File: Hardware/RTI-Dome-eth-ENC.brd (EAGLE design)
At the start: 119.4 x 71.1 mm, 87 parts, among them IC1 24AA128ST, IC3 FT232RL, IC4 REG1117, IC5 74LVC245, IC6 74ABT245, J1 POWERPOLE_POWER45A, U1 W5500, X13 PN61729-S, X9 J1011F21PNL

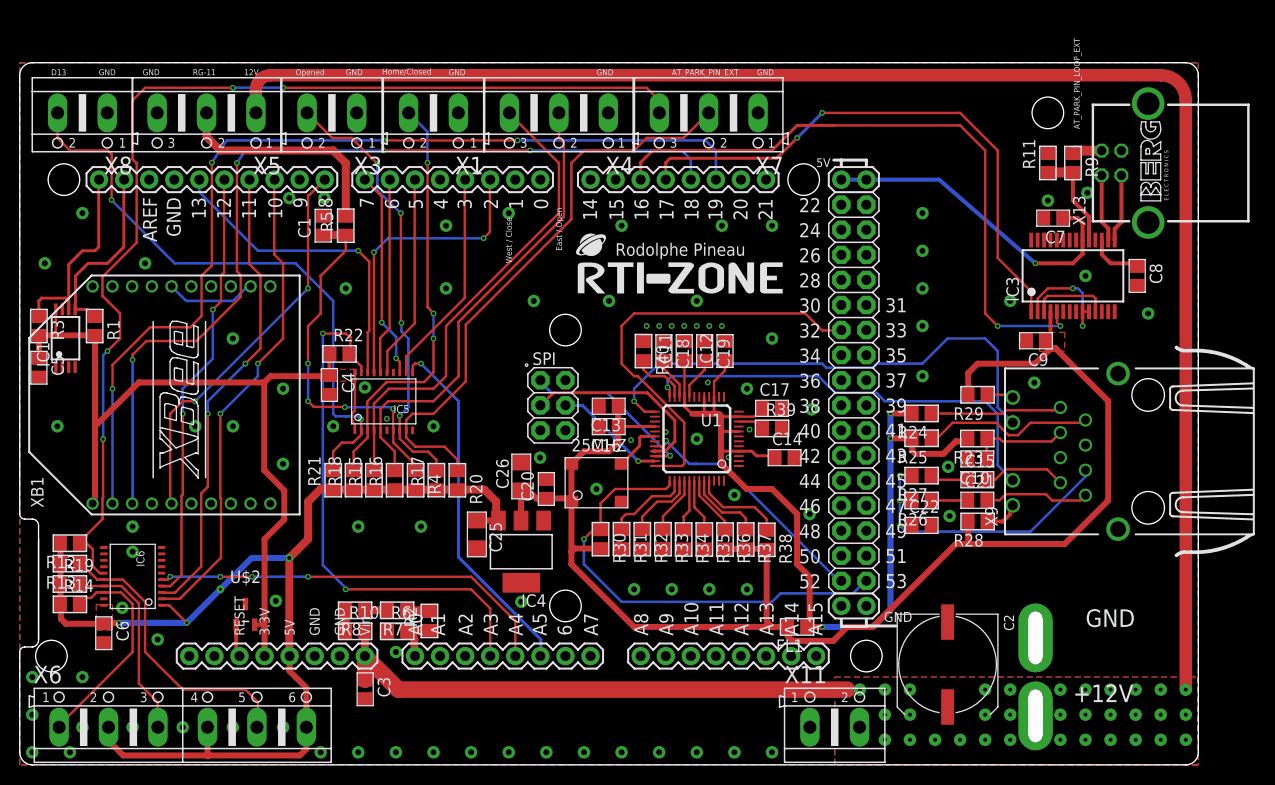
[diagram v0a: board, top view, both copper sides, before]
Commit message: Better homing code. Does necessarily stop at home bug sinf home via an interrupt. I'll add more got to go back home after passing it. It does however return the proper position after homing. Added more board for ENC424J600 ethernet chip. Fix position of the headers.
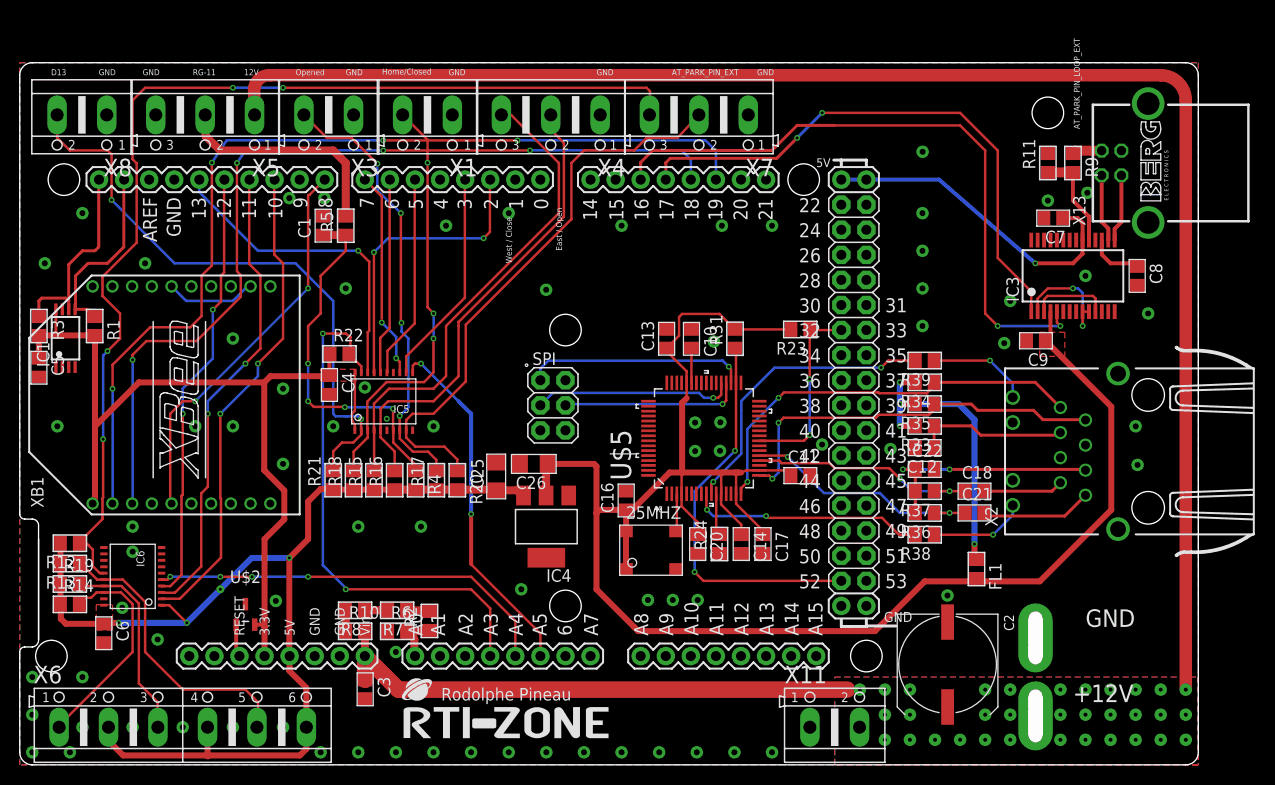
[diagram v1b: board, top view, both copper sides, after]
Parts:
- removed C15: 6.8nF, rti:C0805
- removed C19: 4.7uF, rti:C0805
- removed R25, R26, R27: 49.9 1%, rti:R0805
- removed R28, R29: 330, rti:R0805
- removed R30, R32, R40: 4.7K, rti:R0805
- removed U1: W5500, W5500:LQFP48
- added U$5: ENC424J600-I/PT, Microchip_By_element14_Batch_1:QFP50P1200X1200X120-44N
- C10: value 22nF -> 10uF
- C12: value 100nF -> 10nF
- C18: value 10nF -> 6.8nF
- R23: value 10 1% -> 10K
- R24: value 49.9 1% -> 12.4K 1%
- R31: value 4.7K -> 10K
- R33: value 4.7K -> 10 1%
- R34, R35, R36, R37: value 4.7K -> 49.9 1%
- R38: value 4.7K -> 1K
- R39: value 12.4K 1% -> 1K
- moved U$4 48.4 mm to (38.9, 2.71)
- moved C18 34.5 mm to (96.7, 27.7), turned to 0 degrees
- moved C10 31.4 mm to (68.0, 43.2), turned to 270 degrees
- moved R34 29.1 mm to (91.7, 38.7), turned to 180 degrees
- moved R33 28.9 mm to (91.7, 34.3), turned to 180 degrees
- moved R35 26.2 mm to (91.7, 36.5), turned to 180 degrees
- moved R24 24.4 mm to (70.9, 22.4), turned to 90 degrees
- moved R31 23.3 mm to (72.5, 43.2), turned to 90 degrees
- moved C12 22.5 mm to (91.7, 32.1), turned to 180 degrees
- moved R23 21.1 mm to (79.1, 44.1)
- moved R36 20.4 mm to (91.7, 25.5), turned to 180 degrees
- moved FL1 19.1 mm to (96.9, 19.8), turned to 270 degrees
- moved R37 18.8 mm to (91.7, 27.7), turned to 180 degrees
- moved C11 17.2 mm to (79.1, 29.3), turned to 0 degrees
- moved R39 16.9 mm to (91.7, 41.0), turned to 180 degrees
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- renumbered X9 to X2
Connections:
- removed net N$11: C15.2, X2.7
- removed net N$17 (its old number): U1.26
- removed net N$22: R31.1, U1.38
- removed net N$23: R32.1, U1.39
- removed net N$24: R33.1, U1.40
- removed net N$25: R34.1, U1.41
- removed net N$26: R35.1, U1.42
- removed net N$27: R36.1, U1.43
- removed net N$28: R37.1, U1.44
- removed net N$29: R38.1, U1.45
- removed net N$31: C19.2, U1.20
- removed net N$32: U1.18
- removed net N$33: C18.2, U1.22
- removed net N$34: R39.1, U1.10
- removed net N$35: R40.2, U1.23
- removed net SPD_100: U1.24, X2.11
- removed net XO: U1.31
- new net ACTIVITY: R38.2, U$5.9
- new net N$14: R38.1, X2.12
- new net N$16: C18.2, X2.7
- net +3V3: now also C11.1, C14.1, C17.1, R23.2, R31.2, U$5.12, U$5.15, U$5.18, U$5.4, U$5.44; no longer R28.2, R29.2, R30.2, R36.2, R37.2, R38.2, U1.28
- net AVDD: now also R33.2, R34.2, R35.2; no longer C11.1, C12.1, C14.1, C17.1, R23.2, R24.2, R25.2, U1.11, U1.15, U1.17, U1.21, U1.4, U1.8
- net ETH_CS: now also R31.1, U$5.34; no longer U1.32
- net ETH_RESET: no longer R30.1, U1.37
- net GND: now also C10.1, R24.1, U$5.1, U$5.13, U$5.14, U$5.19, U$5.22, U$5.33, U$5.42, X2.10, X2.11; no longer C10.2, C18.1, C19.1, R31.2, R32.2, R33.2, R34.2, R35.2, R39.2, R40.1, U1.14, U1.16, U1.19, U1.29, U1.3, U1.48, U1.9
- net INT_N: now also R23.1, U$5.24; no longer U1.36
- net LINK_ACK: now also R39.2, U$5.10; no longer U1.25, X2.10
- net N$10: now also R39.1, X2.9; no longer R28.1, X2.12
- net N$13: now also C22.1, R36.2, R37.2, X2.6; no longer C10.1, R23.1, X2.3
- net N$18: now also C12.1, R33.1, X2.3; no longer U1.27
- net N$7: now also R24.2, U$5.11; no longer C22.1, R26.2, R27.2, X2.6
- net N$8: now also C10.2, U$5.43; no longer R29.1, X2.9
- net RXN: now also R36.1, U$5.21; no longer R26.1, U1.5
- net RXP: now also C18.1, R37.1, U$5.20; no longer C15.1, R27.1, U1.6
- net SCLK: now also U$5.37; no longer U1.33
- net SDI: now also U$5.35; no longer U1.34
- net SDO: now also U$5.36; no longer U1.35
- net TXN: now also R35.1, U$5.17; no longer R25.1, U1.1
- net TXP: now also R34.1, U$5.16; no longer R24.1, U1.2
- net XI: now also U$5.3; no longer U1.30
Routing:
- net AVDD: track 96.4 -> 31.6 mm, vias 3 -> 4
- net ETH_RESET: track 46.6 -> 0.00 mm, vias 1 -> 0
- net SPD_100: track 44.3 -> 0.00 mm, vias 1 -> 0
- net +3V3: track 146.1 -> 181.8 mm
- net TXP: track 13.4 -> 41.8 mm, vias 0 -> 2
- net N$7: track 30.8 -> 4.28 mm, vias 3 -> 0
- net INT_N: track 43.4 -> 19.3 mm, vias 0 -> 2
- net ACTIVITY: track 0.00 -> 23.8 mm, vias 0 -> 2
- net TXN: track 17.5 -> 40.3 mm, vias 0 -> 2
- net LINK_ACK: track 51.5 -> 30.0 mm, vias 1 -> 2
- net RXN: track 3.76 -> 24.8 mm, vias 0 -> 2
- net RXP: track 3.92 -> 23.7 mm, vias 0 -> 2
- net N$18: track 0.00 -> 15.5 mm
- net ETH_CS: track 25.5 -> 39.7 mm, vias 1 -> 2
- net N$13: track 10.0 -> 24.2 mm, vias 0 -> 2
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
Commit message: Fix all board for proper header alignement. New code for homing (and calibrating) tested and works.
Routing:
- net INT_N: track 19.3 -> 18.7 mm
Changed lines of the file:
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@@
 <contactref element="25MHZ" pad="2"/>
 <contactref element="C20" pad="2"/>
-<via x="113.03" y="34.29" extent="1-16" drill="0.6" diameter="1.27"/>
-<via x="113.225" y="30.38" extent="1-16" drill="0.6" diameter="1.27"/>
+<via x="113.4" y="34.335" extent="1-16" drill="0.6" diameter="1.27"/>
+<via x="113.4" y="29.295" extent="1-16" drill="0.6" diameter="1.27"/>
 <via x="114.3" y="45.72" extent="1-16" drill="0.6" diameter="1.27"/>
 <via x="88.19975" y="31.9825" extent="1-16" drill="0.6" diameter="1.27"/>
@@
 <wire x1="35.21075" y1="36.79825" x2="35.21075" y2="33.92425" width="0.254" layer="1"/>
 <wire x1="35.21075" y1="33.92425" x2="35.245" y2="33.89" width="0.254" layer="1"/>
-<wire x1="38.7854" y1="65.835" x2="41.30675" y2="63.31365" width="0.254" layer="1"/>
-<wire x1="41.30675" y1="63.31365" x2="41.30675" y2="60.99175" width="0.254" layer="1"/>
+<wire x1="38.7854" y1="65.835" x2="41.30675" y2="63.31365" width="0.254" layer="16"/>
+<wire x1="41.30675" y1="63.31365" x2="41.30675" y2="60.99175" width="0.254" layer="16"/>
 </signal>
 <signal name="BUTTON_WEST_CLOSE_5V">
@@
 <contactref element="R35" pad="1"/>
 <contactref element="U$5" pad="17"/>
-<wire x1="92.615" y1="36.54" x2="96.39" y2="36.54" width="0.3048" layer="1"/>
-<wire x1="96.39" y1="36.54" x2="97.02" y2="35.91" width="0.3048" layer="1"/>
-<wire x1="97.02" y1="35.91" x2="102.69" y2="35.91" width="0.3048" layer="1"/>
-<wire x1="102.69" y1="35.91" x2="103.635" y2="34.965" width="0.3048" layer="1"/>
-<wire x1="103.635" y1="34.965" x2="107.91" y2="34.965" width="0.3048" layer="1"/>
-<wire x1="107.91" y1="34.965" x2="107.95" y2="34.925" width="0.4064" layer="1"/>
 <wire x1="74.9134" y1="29.3158" x2="74.9342" y2="29.295" width="0.254" layer="1"/>
 <via x="76.23" y="28.98" extent="1-16" drill="0.3"/>
-<wire x1="76.86" y1="29.925" x2="76.86" y2="34.65" width="0.254" layer="16"/>
-<via x="76.86" y="34.65" extent="1-16" drill="0.3"/>
-<wire x1="76.86" y1="34.65" x2="77.37" y2="35.16" width="0.254" layer="1"/>
-<wire x1="77.37" y1="35.16" x2="86.72" y2="35.16" width="0.254" layer="1"/>
+<wire x1="76.86" y1="29.925" x2="76.86" y2="34.335" width="0.254" layer="16"/>
+<via x="76.86" y="34.335" extent="1-16" drill="0.3"/>
+<wire x1="76.86" y1="34.335" x2="77.685" y2="35.16" width="0.254" layer="1"/>
+<wire x1="77.685" y1="35.16" x2="86.72" y2="35.16" width="0.254" layer="1"/>
 <wire x1="86.72" y1="35.16" x2="87.02" y2="35.46" width="0.254" layer="1"/>
 <wire x1="87.02" y1="35.46" x2="92.1" y2="35.46" width="0.254" layer="1"/>
@@
 <wire x1="76.86" y1="29.925" x2="76.86" y2="29.61" width="0.254" layer="16"/>
 <wire x1="76.86" y1="29.61" x2="76.23" y2="28.98" width="0.254" layer="16"/>
+<wire x1="92.615" y1="36.54" x2="99.225" y2="36.54" width="0.254" layer="1"/>
+<wire x1="99.225" y1="36.54" x2="99.855" y2="35.91" width="0.254" layer="1"/>
+<wire x1="99.855" y1="35.91" x2="102.69" y2="35.91" width="0.254" layer="1"/>
+<wire x1="102.69" y1="35.91" x2="103.635" y2="34.965" width="0.254" layer="1"/>
+<wire x1="103.635" y1="34.965" x2="107.91" y2="34.965" width="0.254" layer="1"/>
+<wire x1="107.91" y1="34.965" x2="107.95" y2="34.925" width="0.254" layer="1"/>
 </signal>
 <signal name="RXP">
@@
 <contactref element="R34" pad="1"/>
 <contactref element="U$5" pad="16"/>
-<wire x1="92.615" y1="38.745" x2="102.86" y2="38.745" width="0.3048" layer="1"/>
-<wire x1="102.86" y1="38.745" x2="105.41" y2="36.195" width="0.3048" layer="1"/>
 <wire x1="73.0592" y1="27.4616" x2="73.0592" y2="28.0142" width="0.254" layer="1"/>
 <wire x1="73.0592" y1="28.0142" x2="73.71" y2="28.665" width="0.254" layer="1"/>
 <via x="73.71" y="28.665" extent="1-16" drill="0.3"/>
 <wire x1="73.71" y1="28.665" x2="73.71" y2="34.02" width="0.254" layer="16"/>
-<wire x1="73.71" y1="34.02" x2="76.86" y2="37.17" width="0.254" layer="16"/>
-<via x="76.86" y="37.17" extent="1-16" drill="0.3"/>
-<wire x1="76.86" y1="37.17" x2="77.41" y2="37.72" width="0.254" layer="1"/>
-<wire x1="77.41" y1="37.72" x2="86.98" y2="37.72" width="0.254" layer="1"/>
-<wire x1="86.98" y1="37.72" x2="87.06" y2="37.64" width="0.254" layer="1"/>
-<wire x1="87.06" y1="37.64" x2="91.87" y2="37.64" width="0.254" layer="1"/>
 <wire x1="91.87" y1="37.64" x2="92.615" y2="38.385" width="0.254" layer="1"/>
 <wire x1="92.615" y1="38.385" x2="92.615" y2="38.745" width="0.254" layer="1"/>
+<wire x1="91.87" y1="37.64" x2="88.985" y2="37.64" width="0.254" layer="1"/>
+<wire x1="88.985" y1="37.64" x2="87.885" y2="36.54" width="0.254" layer="1"/>
+<via x="87.885" y="36.54" extent="1-16" drill="0.3"/>
+<wire x1="87.885" y1="36.54" x2="87.85" y2="36.54" width="0.254" layer="16"/>
+<wire x1="87.85" y1="36.54" x2="86.47" y2="35.16" width="0.254" layer="16"/>
+<wire x1="86.47" y1="35.16" x2="74.85" y2="35.16" width="0.254" layer="16"/>
+<wire x1="74.85" y1="35.16" x2="73.71" y2="34.02" width="0.254" layer="16"/>
+<wire x1="92.615" y1="38.385" x2="103.22" y2="38.385" width="0.254" layer="1"/>
+<wire x1="103.22" y1="38.385" x2="105.41" y2="36.195" width="0.254" layer="1"/>
 </signal>
 <signal name="INT_N">
@@
 <wire x1="80.015" y1="39.065" x2="80.01" y2="39.06" width="0.254" layer="1"/>
 <via x="80.01" y="39.06" extent="1-16" drill="0.3"/>
-<wire x1="80.01" y1="39.06" x2="80.01" y2="33.39" width="0.254" layer="16"/>
-<via x="80.01" y="33.39" extent="1-16" drill="0.3"/>
-<wire x1="80.01" y1="33.39" x2="79.441" y2="32.821" width="0.254" layer="1"/>
-<wire x1="79.441" y1="32.821" x2="74.9134" y2="32.821" width="0.254" layer="1"/>
+<via x="80.01" y="36.855" extent="1-16" drill="0.3"/>
+<wire x1="74.9134" y1="32.821" x2="75.976" y2="32.821" width="0.254" layer="1"/>
+<wire x1="75.976" y1="32.821" x2="76.23" y2="33.075" width="0.254" layer="1"/>
+<wire x1="76.23" y1="33.075" x2="76.23" y2="35.595" width="0.254" layer="1"/>
+<wire x1="76.23" y1="35.595" x2="77.49" y2="36.855" width="0.254" layer="1"/>
+<wire x1="77.49" y1="36.855" x2="80.01" y2="36.855" width="0.254" layer="1"/>
+<wire x1="80.015" y1="39.065" x2="80.015" y2="36.86" width="0.254" layer="1"/>
+<wire x1="80.015" y1="36.86" x2="80.01" y2="36.855" width="0.254" layer="1"/>
 </signal>
 <signal name="XI">
@@
 <contactref element="X2" pad="7"/>
 <contactref element="C18" pad="2"/>
-<wire x1="97.655" y1="27.72" x2="104.555" y2="27.72" width="0.3048" layer="1"/>
-<wire x1="104.555" y1="27.72" x2="105.41" y2="28.575" width="0.3048" layer="1"/>
+<wire x1="97.655" y1="27.72" x2="104.555" y2="27.72" width="0.254" layer="1"/>
+<wire x1="104.555" y1="27.72" x2="105.41" y2="28.575" width="0.254" layer="1"/>
 </signal>
 <signal name="N$17">
 <contactref element="X2" pad="8"/>
 <contactref element="C21" pad="2"/>
-<wire x1="107.95" y1="27.305" x2="105.845" y2="25.2" width="0.3048" layer="1"/>
-<wire x1="105.845" y1="25.2" x2="98.28" y2="25.2" width="0.3048" layer="1"/>
+<wire x1="107.95" y1="27.305" x2="105.845" y2="25.2" width="0.254" layer="1"/>
+<wire x1="105.845" y1="25.2" x2="98.28" y2="25.2" width="0.254" layer="1"/>
 <wire x1="98.28" y1="25.2" x2="97.965" y2="25.515" width="0.3048" layer="1"/>
 <wire x1="97.965" y1="25.515" x2="97.655" y2="25.515" width="0.3048" layer="1"/>

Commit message: PCB optimisation
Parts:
- moved C25 50.2 mm to (89.5, 58.0)
- moved C26 48.5 mm to (92.0, 58.0), turned to 90 degrees
- moved IC4 46.8 mm to (91.7, 51.0)
- moved FL1 23.6 mm to (95.5, 43.4), turned to 0 degrees
- moved C16 5.09 mm to (59.5, 22.1), turned to 270 degrees
- moved C9 3.34 mm to (106.2, 42.4), turned to 0 degrees
- moved C13 0.31 mm to (65.8, 43.2)
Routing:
- net +3V3: track 181.8 -> 170.7 mm
- net AVDD: track 31.6 -> 20.6 mm
